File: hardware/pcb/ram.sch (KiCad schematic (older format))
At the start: 12 parts, among them U100 XC6SLX16-FTG256, U200 IS66WVE4M16

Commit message: vbh: pcb layout
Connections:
- net labels added: LCD_D0, LCD_D1, LCD_D10, LCD_D11, LCD_D12, LCD_D13, LCD_D14, LCD_D15, LCD_D16, LCD_D17, LCD_D2, LCD_D3, LCD_D4, LCD_D5, LCD_D6, LCD_D7, LCD_D8, LCD_D9, LCD_DE, LCD_HS, LCD_PCLK, LCD_VS
- wire segments 147 -> 169
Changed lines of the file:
@@
 NoConn ~ 1700 5500
 NoConn ~ 1700 5600
+Text GLabel 1150 4900 0    50   Input ~ 0
+LCD_D0
+Text GLabel 1150 5000 0    50   Input ~ 0
+LCD_D1
+Text GLabel 1150 5100 0    50   Input ~ 0
+LCD_D2
+Text GLabel 1150 5200 0    50   Input ~ 0
+LCD_D3
+Text GLabel 1150 5300 0    50   Input ~ 0
+LCD_D4
+Text GLabel 1150 5400 0    50   Input ~ 0
+LCD_D5
+Text GLabel 1150 5500 0    50   Input ~ 0
+LCD_D6
+Text GLabel 1150 5600 0    50   Input ~ 0
+LCD_D7
+Text GLabel 1150 5700 0    50   Input ~ 0
+LCD_D8
+Text GLabel 1150 5800 0    50   Input ~ 0
+LCD_D9
+Text GLabel 1150 5900 0    50   Input ~ 0
+LCD_D10
+Text GLabel 1150 6000 0    50   Input ~ 0
+LCD_D11
+Text GLabel 1150 6100 0    50   Input ~ 0
+LCD_D12
+Text GLabel 1150 6200 0    50   Input ~ 0
+LCD_D13
+Text GLabel 1150 6300 0    50   Input ~ 0
+LCD_D14
+Text GLabel 1150 6400 0    50   Input ~ 0
+LCD_D15
+Text GLabel 1150 6500 0    50   Input ~ 0
+LCD_D16
+Text GLabel 1150 6600 0    50   Input ~ 0
+LCD_D17
+Text GLabel 1150 7400 0    50   Input ~ 0
+LCD_PCLK
+Text GLabel 1150 7500 0    50   Input ~ 0
+LCD_DE
+Text GLabel 1150 7600 0    50   Input ~ 0
+LCD_VS
+Text GLabel 1150 7700 0    50   Input ~ 0
+LCD_HS
+Wire Wire Line
+	1150 4900 1350 4900
+Wire Wire Line
+	1150 5000 1350 5000
+Wire Wire Line
+	1150 5100 1350 5100
+Wire Wire Line
+	1150 5200 1350 5200
+Wire Wire Line
+	1150 5300 1350 5300
+Wire Wire Line
+	1150 5400 1350 5400
+Wire Wire Line
+	1150 5500 1350 5500
+Wire Wire Line
+	1150 5600 1350 5600
+Wire Wire Line
+	1150 5700 1350 5700
+Wire Wire Line
+	1150 5800 1350 5800
+Wire Wire Line
+	1150 5900 1350 5900
+Wire Wire Line
+	1150 6000 1350 6000
+Wire Wire Line
+	1150 6100 1350 6100
+Wire Wire Line
+	1150 6200 1350 6200
+Wire Wire Line
+	1150 6300 1350 6300
+Wire Wire Line
+	1150 6400 1350 6400
+Wire Wire Line
+	1150 6500 1350 6500
+Wire Wire Line
+	1150 6600 1350 6600
+Wire Wire Line
+	1150 7400 1350 7400
+Wire Wire Line
+	1150 7500 1350 7500
+Wire Wire Line
+	1150 7600 1350 7600
+Wire Wire Line
+	1150 7700 1350 7700
 $EndSCHEMATC

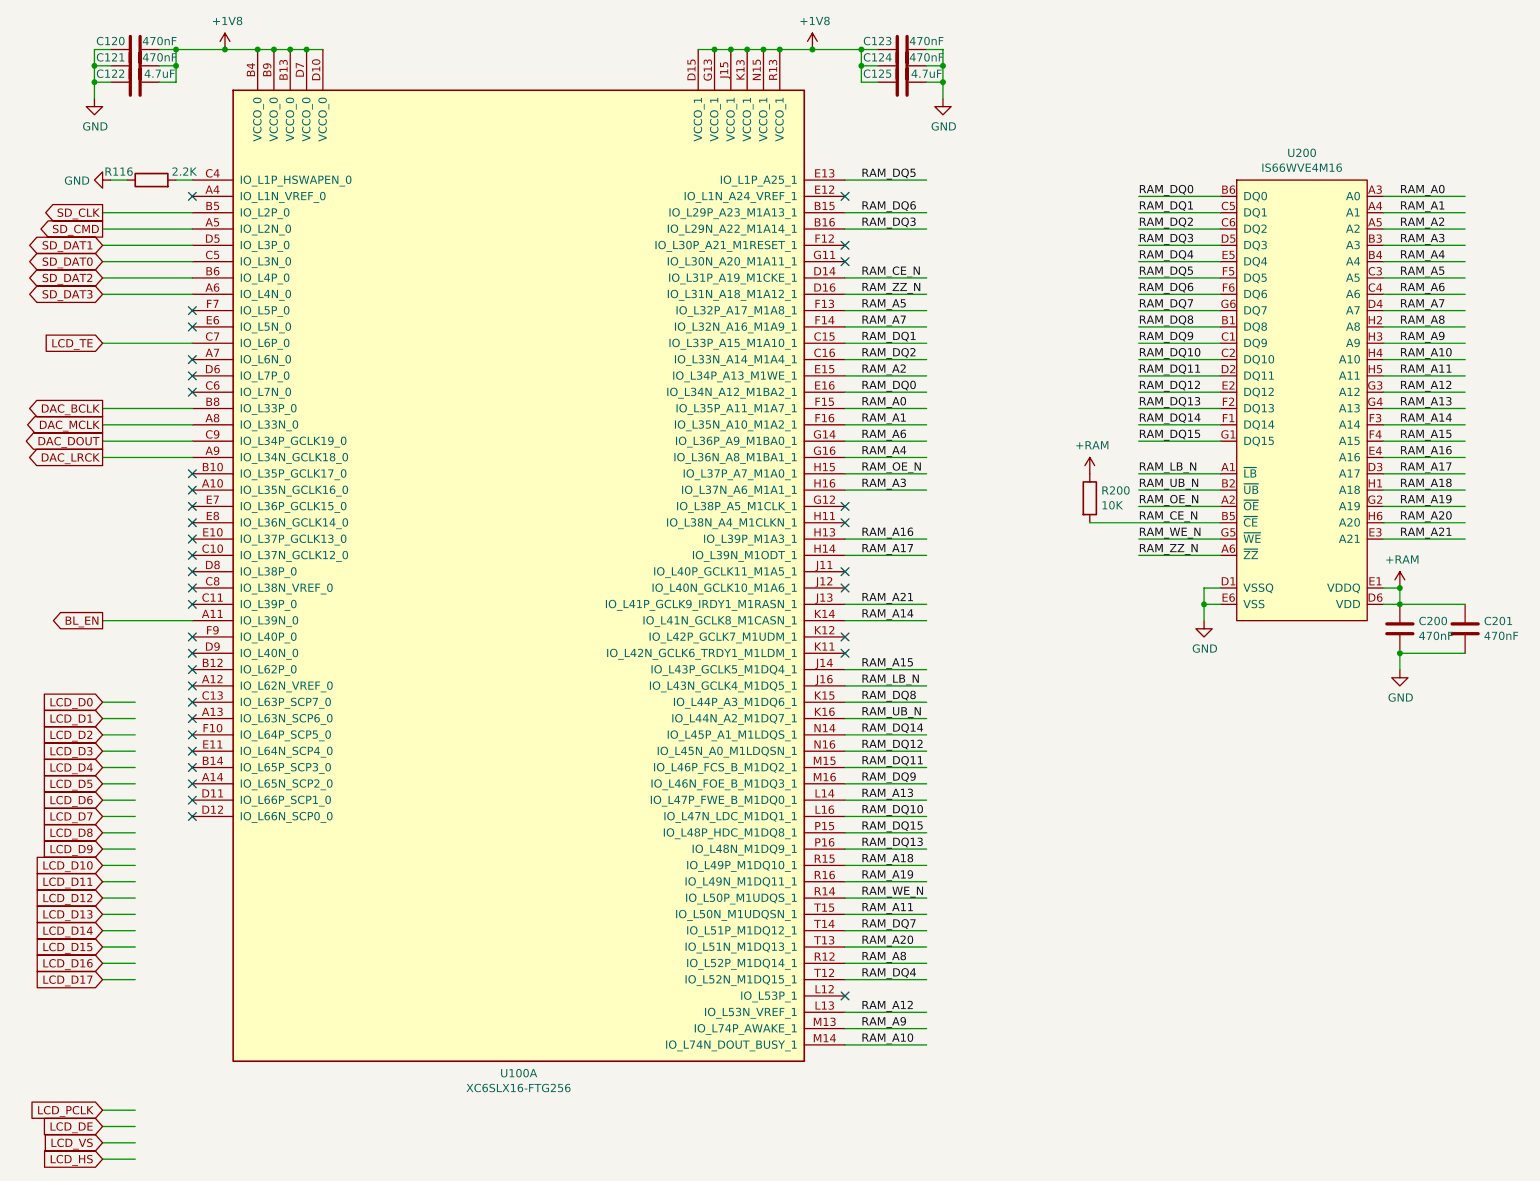
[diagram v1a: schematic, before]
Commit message: pcb: working on ram/ lcd routing
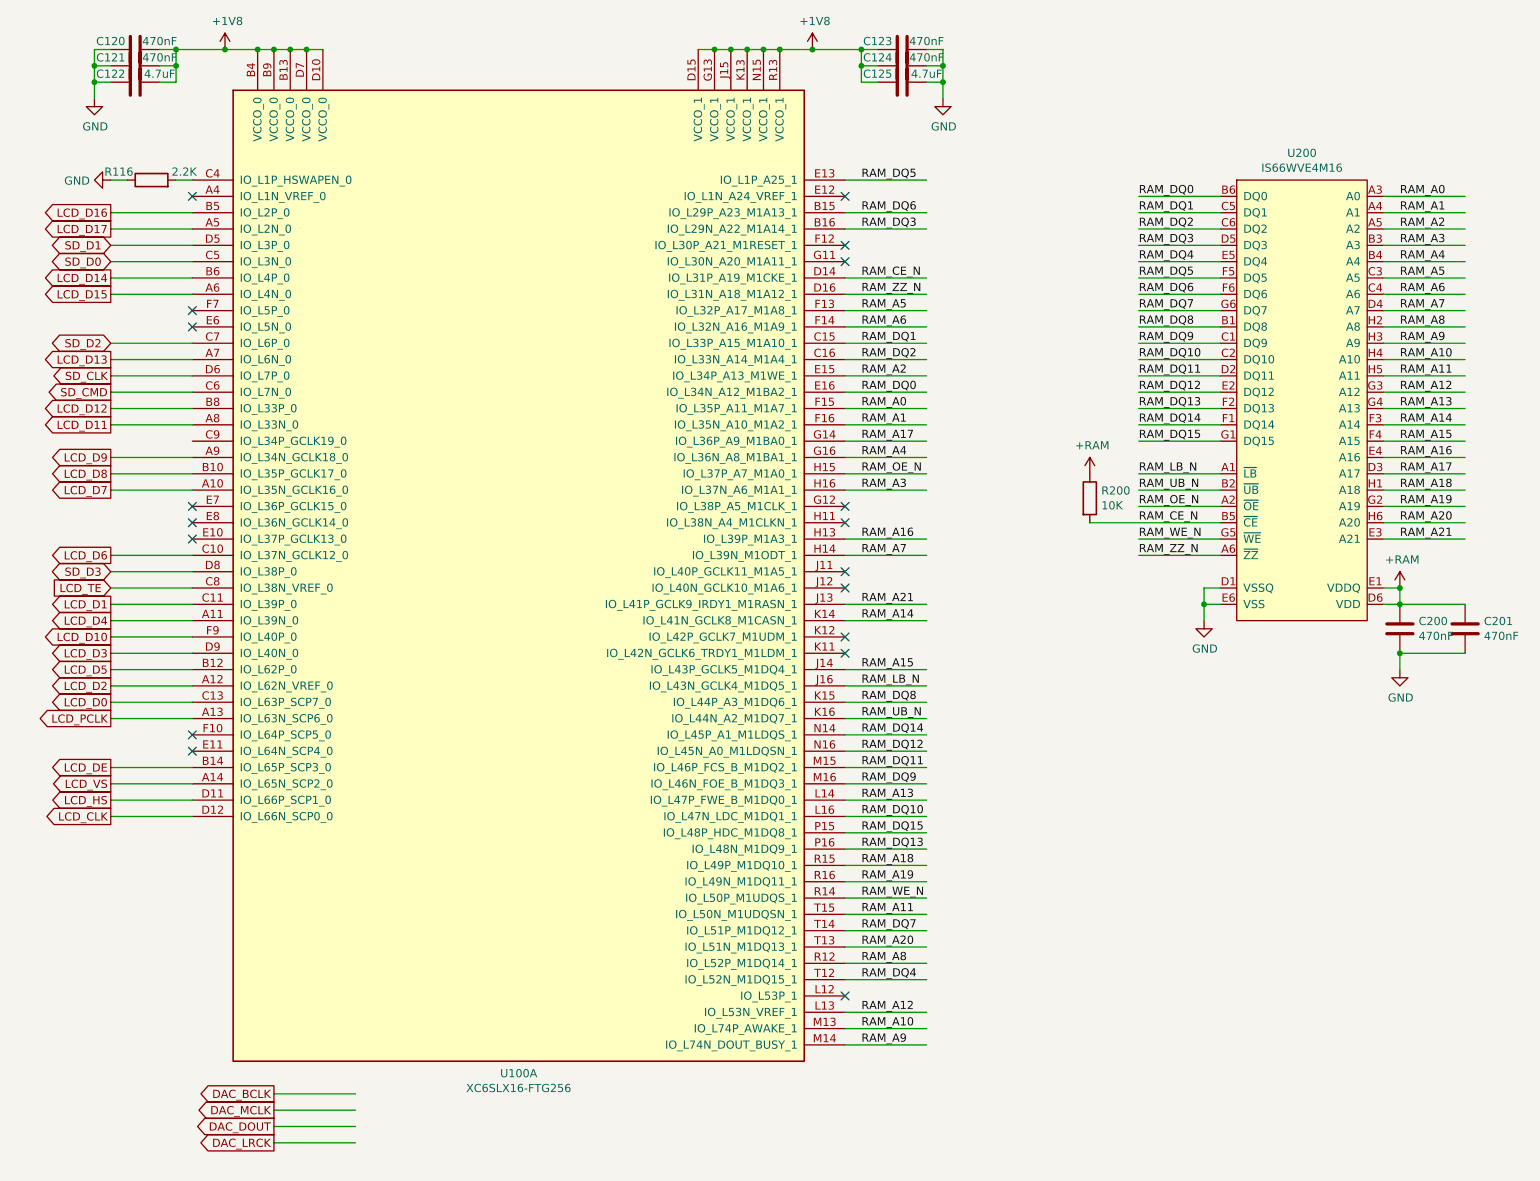
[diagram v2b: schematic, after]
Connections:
- net labels added: LCD_CLK, SD_D0, SD_D1, SD_D2, SD_D3
- net labels removed: BL_EN, SD_DAT0, SD_DAT1, SD_DAT2, SD_DAT3
- no-connect marks 37 -> 18

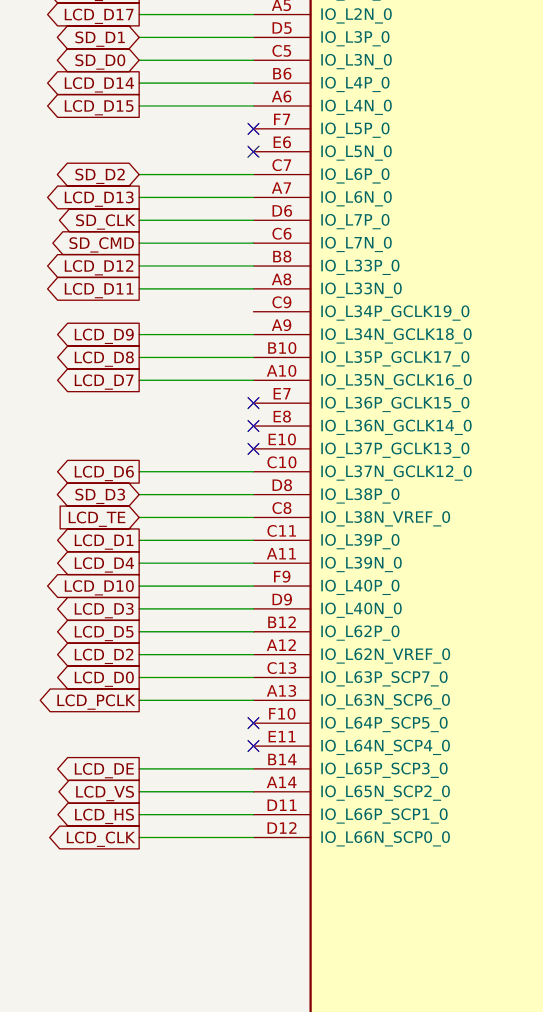
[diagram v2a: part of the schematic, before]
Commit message: pcb: routing lcd section
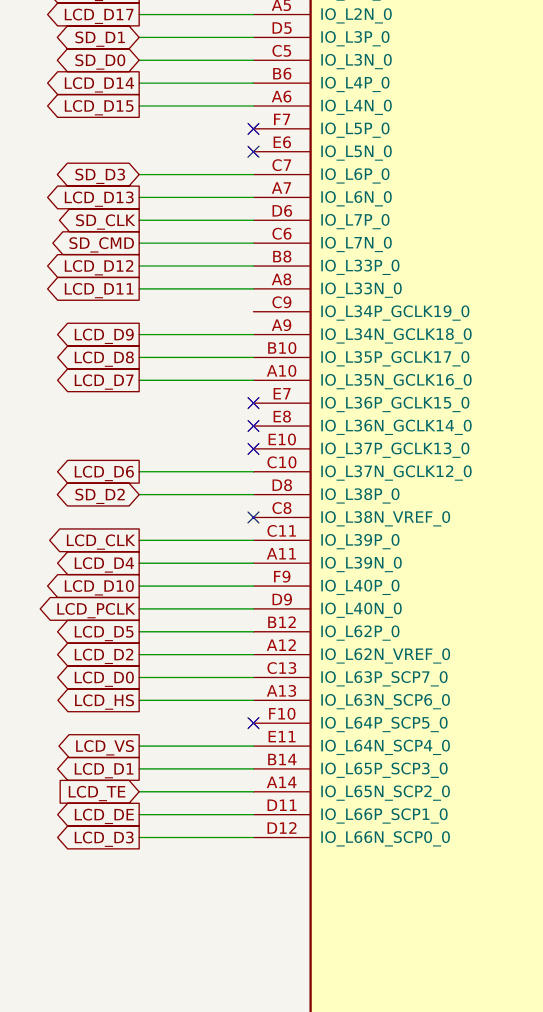
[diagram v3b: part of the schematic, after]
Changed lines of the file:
@@
 SD_D0
 Text GLabel 1200 2700 0    50   BiDi ~ 0
-SD_D2
-Text GLabel 1200 4100 0    50   BiDi ~ 0
 SD_D3
-Text GLabel 1200 4200 0    50   Input ~ 0
+Text GLabel 1200 5400 0    50   Input ~ 0
 LCD_TE
 Text GLabel 2200 7300 0    50   Output ~ 0
@@
 NoConn ~ 1700 3900
 NoConn ~ 1700 5100
-NoConn ~ 1700 5200
+NoConn ~ 1700 4200
 Text GLabel 1200 4900 0    50   Output ~ 0
 LCD_D0
-Text GLabel 1200 4300 0    50   Output ~ 0
+Text GLabel 1200 5300 0    50   Output ~ 0
 LCD_D1
 Text GLabel 1200 4800 0    50   Output ~ 0
 LCD_D2
-Text GLabel 1200 4600 0    50   Output ~ 0
+Text GLabel 1200 5600 0    50   Output ~ 0
 LCD_D3
 Text GLabel 1200 4400 0    50   Output ~ 0
@@
 Text GLabel 1200 2000 0    50   Output ~ 0
 LCD_D17
+Text GLabel 1200 4600 0    50   Output ~ 0
+LCD_PCLK
+Text GLabel 1200 5500 0    50   Output ~ 0
+LCD_DE
 Text GLabel 1200 5000 0    50   Output ~ 0
-LCD_PCLK
-Text GLabel 1200 5300 0    50   Output ~ 0
-LCD_DE
-Text GLabel 1200 5400 0    50   Output ~ 0
-LCD_VS
-Text GLabel 1200 5500 0    50   Output ~ 0
 LCD_HS
-Text GLabel 1200 5600 0    50   Output ~ 0
-LCD_CLK
 Wire Wire Line
 	5300 900  5500 900
@@
 	1200 2200 1700 2200
 Wire Wire Line
-	1200 4200 1700 4200
-Wire Wire Line
-	1200 4100 1700 4100
+	1200 5400 1700 5400
 Wire Wire Line
 	1200 2700 1700 2700
@@
 	1200 4400 1700 4400
 Wire Wire Line
-	1200 4600 1700 4600
+	1200 5600 1700 5600
 Wire Wire Line
 	1200 4800 1700 4800
 Wire Wire Line
-	1200 4300 1700 4300
+	1200 5300 1700 5300
 Wire Wire Line
 	1200 4900 1700 4900
 Wire Wire Line
-	1200 5000 1700 5000
-Wire Wire Line
-	1200 5300 1700 5300
-Wire Wire Line
-	1200 5400 1700 5400
+	1200 4600 1700 4600
 Wire Wire Line
 	1200 5500 1700 5500
 Wire Wire Line
-	1200 5600 1700 5600
+	1200 5000 1700 5000
 Wire Wire Line
 	1200 4000 1700 4000
@@
 Text GLabel 1200 4700 0    50   Output ~ 0
 LCD_D5
+Wire Wire Line
+	1200 4300 1700 4300
+Text GLabel 1200 4300 0    50   Output ~ 0
+LCD_CLK
+Text GLabel 1200 5200 0    50   Output ~ 0
+LCD_VS
+Wire Wire Line
+	1200 5200 1700 5200
+Wire Wire Line
+	1200 4100 1700 4100
+Text GLabel 1200 4100 0    50   BiDi ~ 0
+SD_D2
 $EndSCHEMATC
